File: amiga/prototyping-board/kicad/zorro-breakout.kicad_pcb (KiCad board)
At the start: 4 copper layers, 180 x 107.6 mm, 13 parts, among them J1 Zorro-II 100, J10 RESERVED / LEGACY, J2 ADDRESS, J3 DATA, J4 BUS CONTROL, J5 AUTOCONFIG / SLOT CONTROL, J6 INTERRUPTS, J7 DMA / ARBITRATION, J8 CLOCKS, J9 POWER

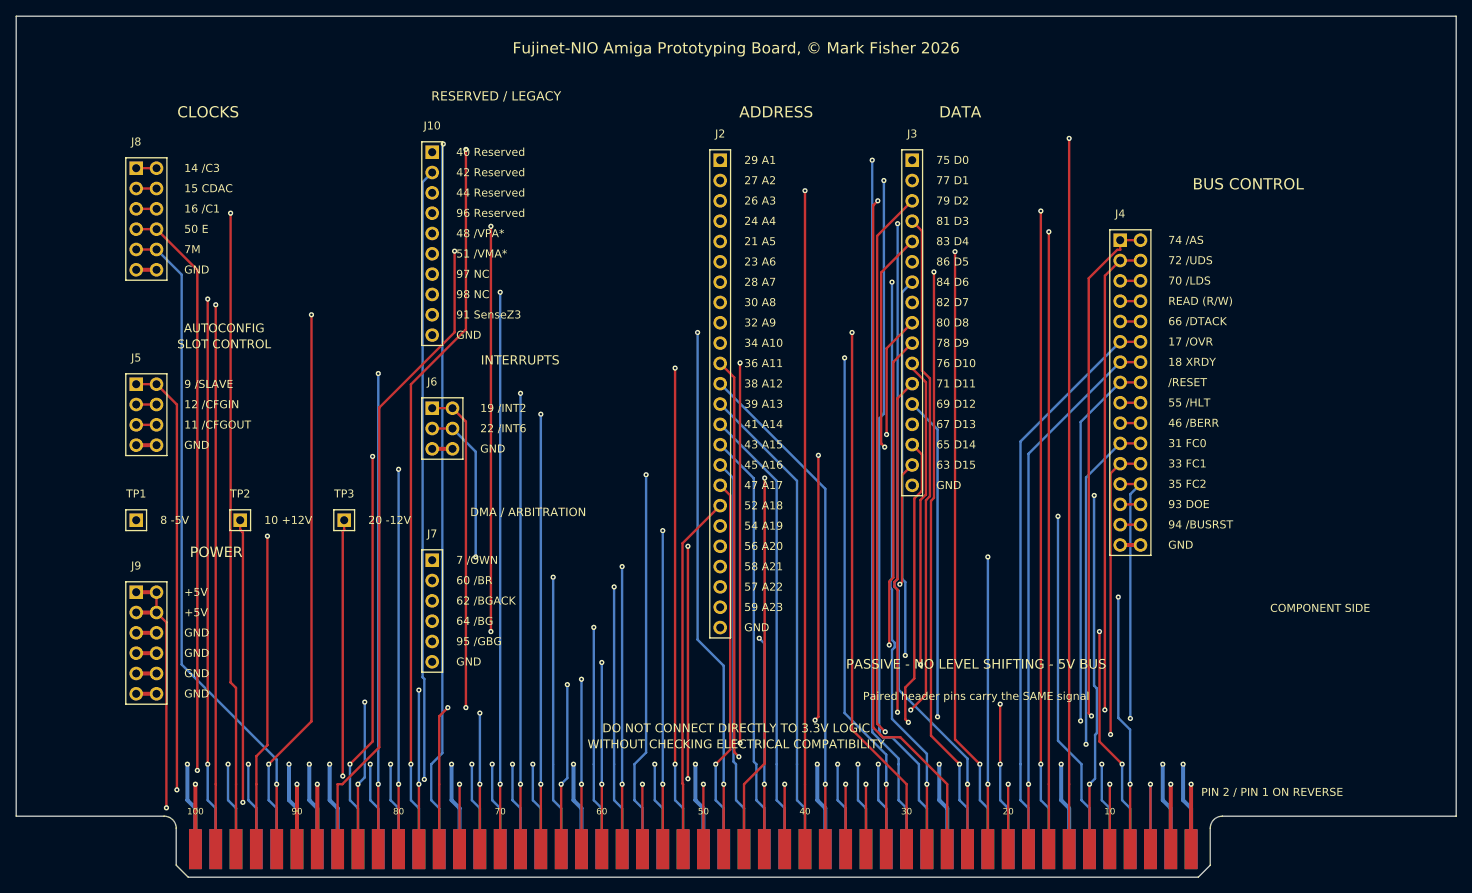
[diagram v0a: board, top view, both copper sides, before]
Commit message: Changed to 2 layer design
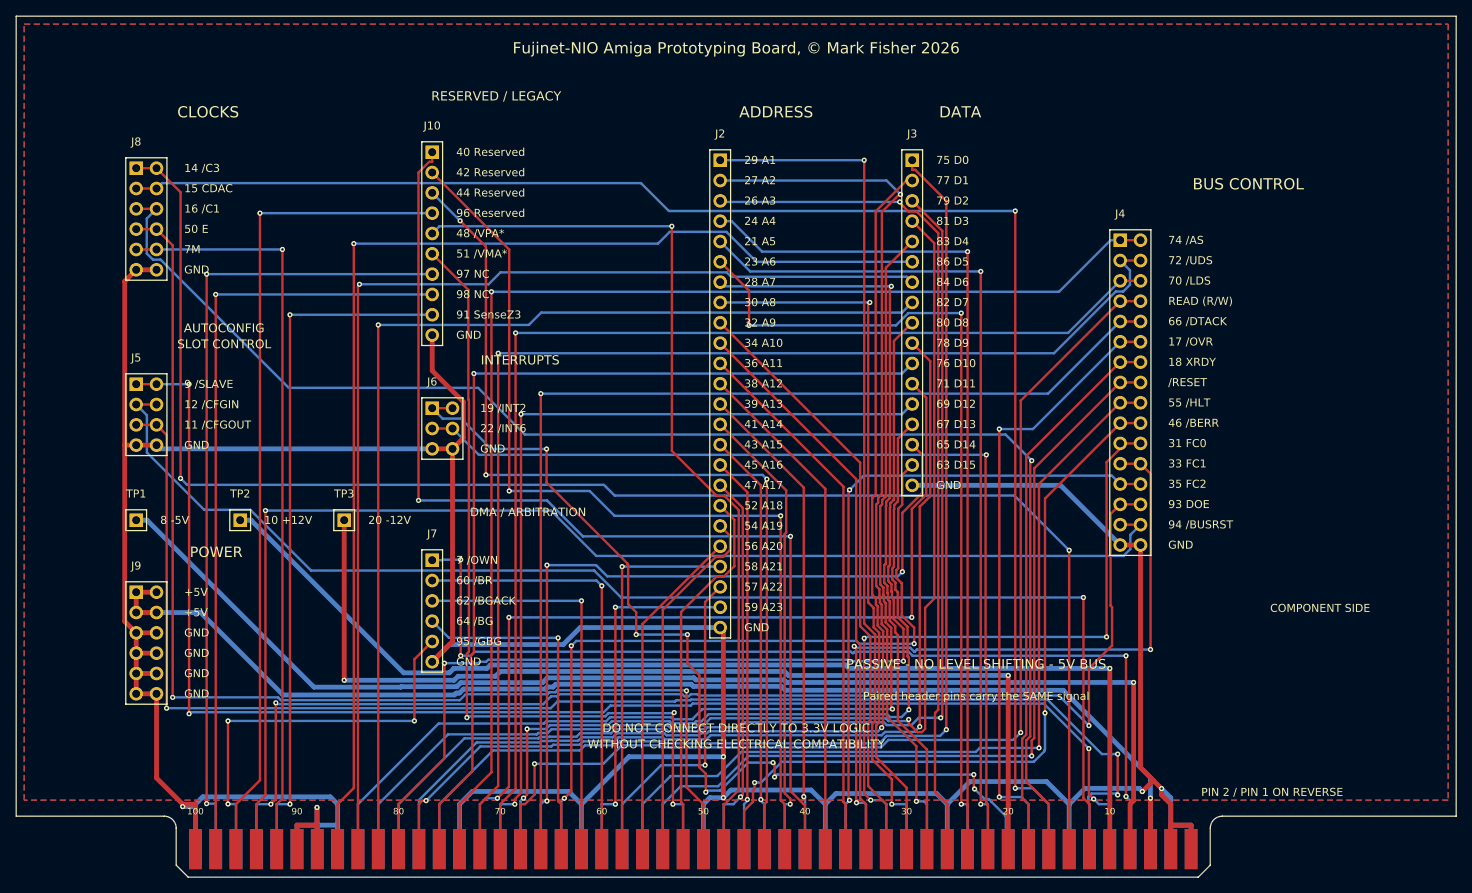
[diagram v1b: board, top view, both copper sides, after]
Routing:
- net GND: track 193.3 -> 528.0 mm, vias 17 -> 6
- net +5V: track 173.2 -> 156.9 mm, vias 2 -> 1
- net +12V: track 153.2 -> 139.8 mm, vias 2 -> 1
- net CFGOUT_N: track 163.2 -> 176.3 mm, vias 1 -> 3
- net C1_N: track 192.4 -> 180.0 mm
- net C3_N: track 207.0 -> 194.7 mm, vias 1 -> 2
- net DOE: track 145.4 -> 156.4 mm, vias 1 -> 3
- net RESERVED_42: track 131.5 -> 120.9 mm
- net BUSRST_N: track 149.4 -> 159.7 mm
- net CLK7M: track 83.7 -> 93.5 mm
- net D5: track 138.9 -> 148.5 mm
- net FC1: track 81.2 -> 90.3 mm, vias 2 -> 3
- net D1: track 148.1 -> 139.5 mm, vias 2 -> 1
- net LEGACY_VPA_N: track 104.5 -> 113.1 mm, vias 2 -> 1
- net GBG_N: track 42.9 -> 51.2 mm, vias 1 -> 3
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- added copper zone on B.Cu, net GND
- added copper zone on F.Cu, net GND
- removed copper zone on In1.Cu, net GND
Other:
- copper layers 4 -> 2
